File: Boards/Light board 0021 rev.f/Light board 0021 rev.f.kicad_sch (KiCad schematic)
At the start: 40 parts, among them J1 card edge, J2 light connector, Q1 TIP130A, U1 2.2K, U1 6821, U2 2.2K, U4 ULN2003A, U5 7406, U6 Board Select, U8 4.7K

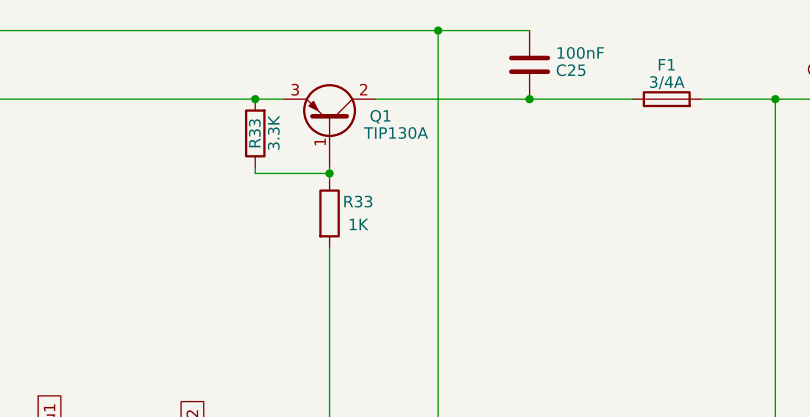
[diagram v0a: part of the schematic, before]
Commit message: revisions from real life boards
tip130a is actually tip30a, widened holes for crystal, widened holes for big power resistor, fixed cpu board LED resistors
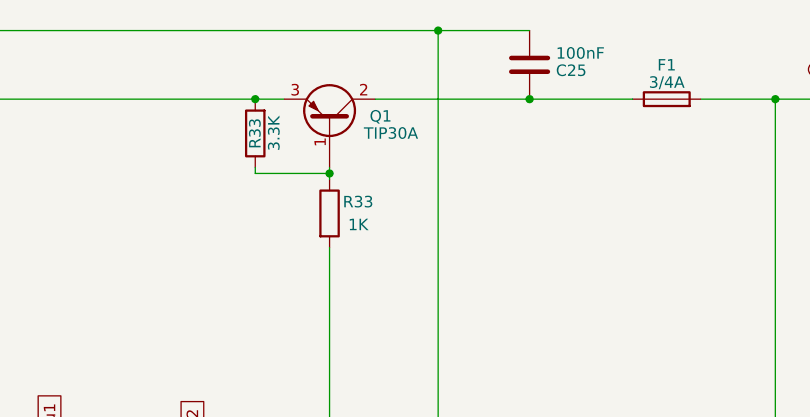
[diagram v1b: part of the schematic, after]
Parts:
- Q1: value TIP130A -> TIP30A
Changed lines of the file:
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@@
       (effects (font (size 1.27 1.27)) (justify left))
     )
-    (property "Value" "TIP130A" (at 177.8 31.75 90)
+    (property "Value" "TIP30A" (at 177.8 31.75 90)
       (effects (font (size 1.27 1.27)) (justify left))
     )
